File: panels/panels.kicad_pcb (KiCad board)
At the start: 2 copper layers, 103 x 63 mm, 13 parts, among them J1 Barrel_Jack_Switch, J2 Barrel_Jack_Switch, J3 Barrel_Jack_Switch, J4 Barrel_Jack_Switch, J5 XLR3

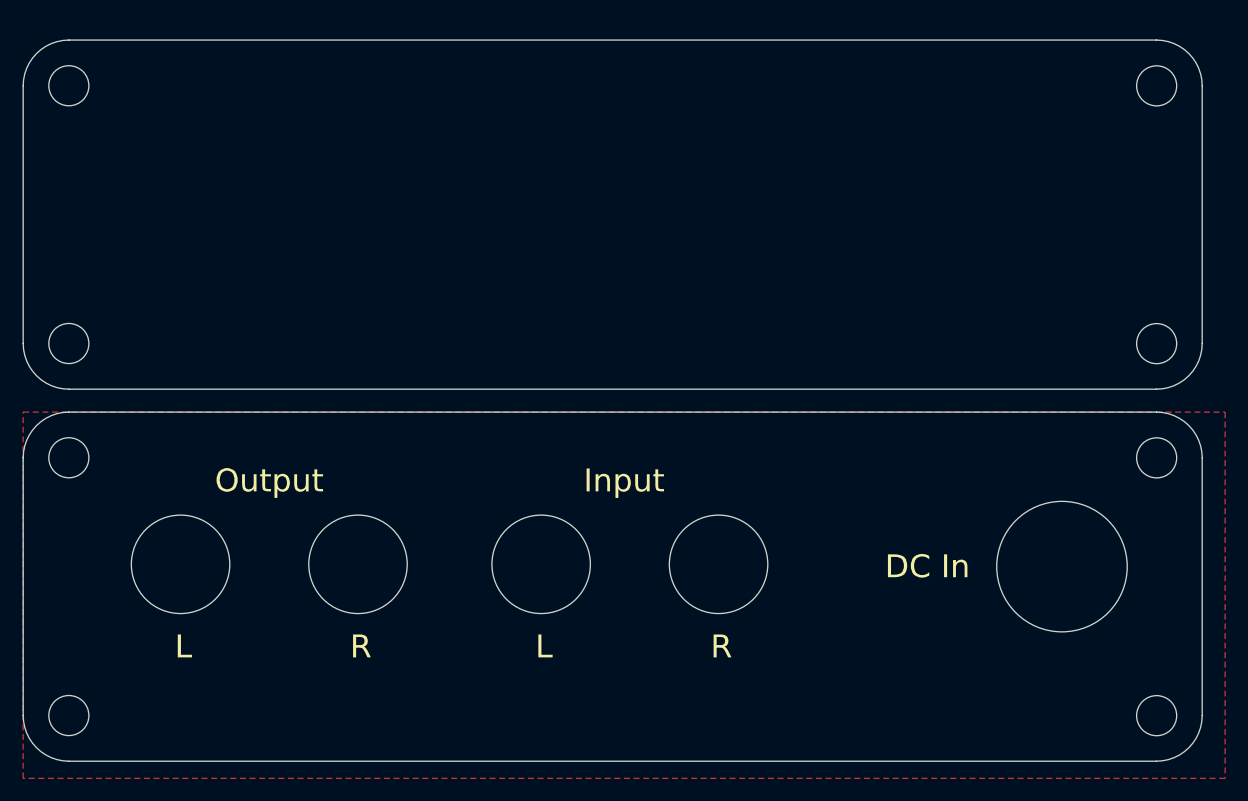
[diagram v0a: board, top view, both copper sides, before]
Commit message: Update panels with custom footprints
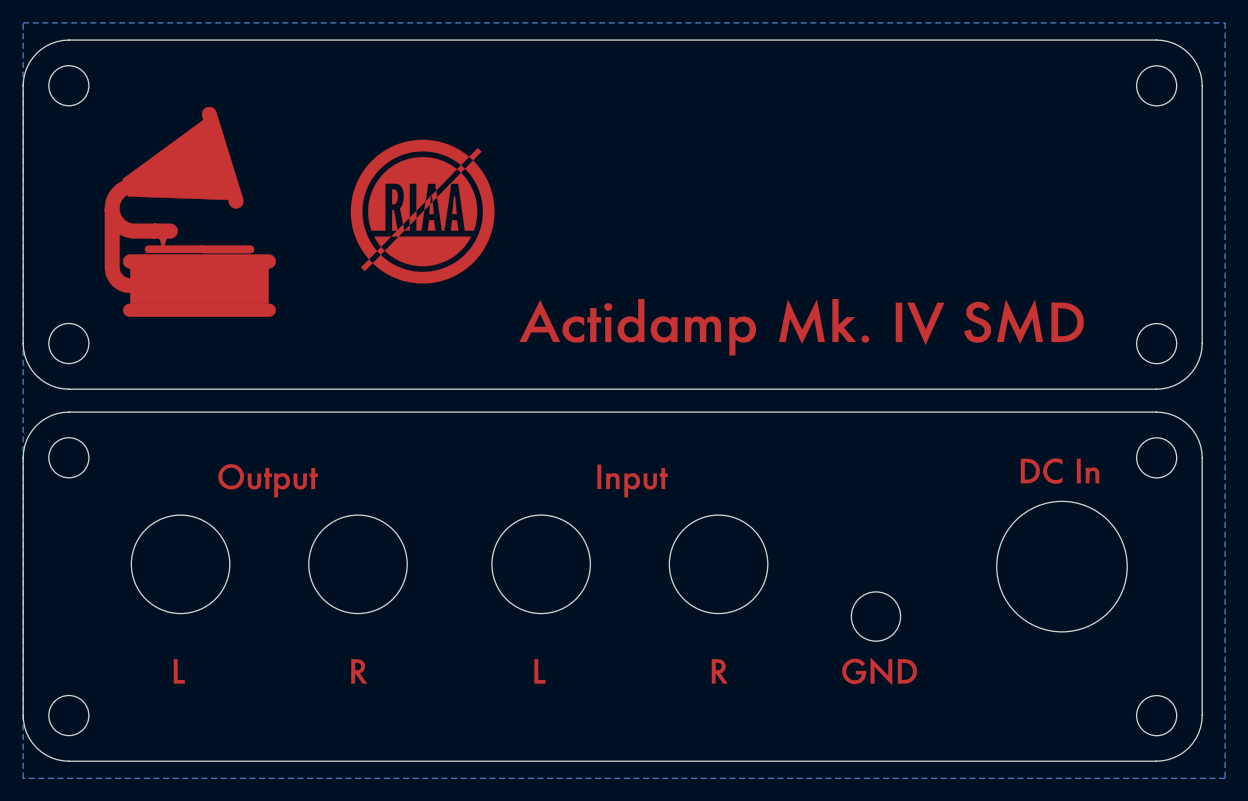
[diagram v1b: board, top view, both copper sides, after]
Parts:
- added Grp1: Logos, actidamp-mk4-smd:FP_Logo, F.Cu at (70.0, 74.0)
- added Grp10: DC In, actidamp-mk4-smd:BP_text_DC_In, F.Cu at (146.5, 95.5)
- added Grp2: Text, actidamp-mk4-smd:FP_text, F.Cu at (123.0, 82.0)
- added Grp3: L, actidamp-mk4-smd:BP_text_L, F.Cu at (72.5, 113.0)
- added Grp4: Output, actidamp-mk4-smd:BP_text_output, F.Cu at (76.5, 96.0)
- added Grp5: R, actidamp-mk4-smd:BP_text_R, F.Cu at (88.0, 113.0)
- added Grp6: L, actidamp-mk4-smd:BP_text_L, F.Cu at (104.0, 113.0)
- added Grp7: Input, actidamp-mk4-smd:BP_text_input, F.Cu at (109.5, 96.0)
- added Grp8: R, actidamp-mk4-smd:BP_text_R, F.Cu at (119.5, 113.0)
- added Grp9: GND, actidamp-mk4-smd:BP_text_GND, F.Cu at (131.0, 113.0)
- added H9: GroundLug, MountingHole:MountingHole_4.3mm_M4, F.Cu at (129.5, 107.9)
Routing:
- added copper zone on B.Cu, net (none)
- removed copper zone on F.Cu, net (none)
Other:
- board text removed: "DC In"
- board text removed: "Input"
- board text removed: "L"
- board text removed: "Output"
- board text removed: "R"

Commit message: Use only mask layer for FB/BP
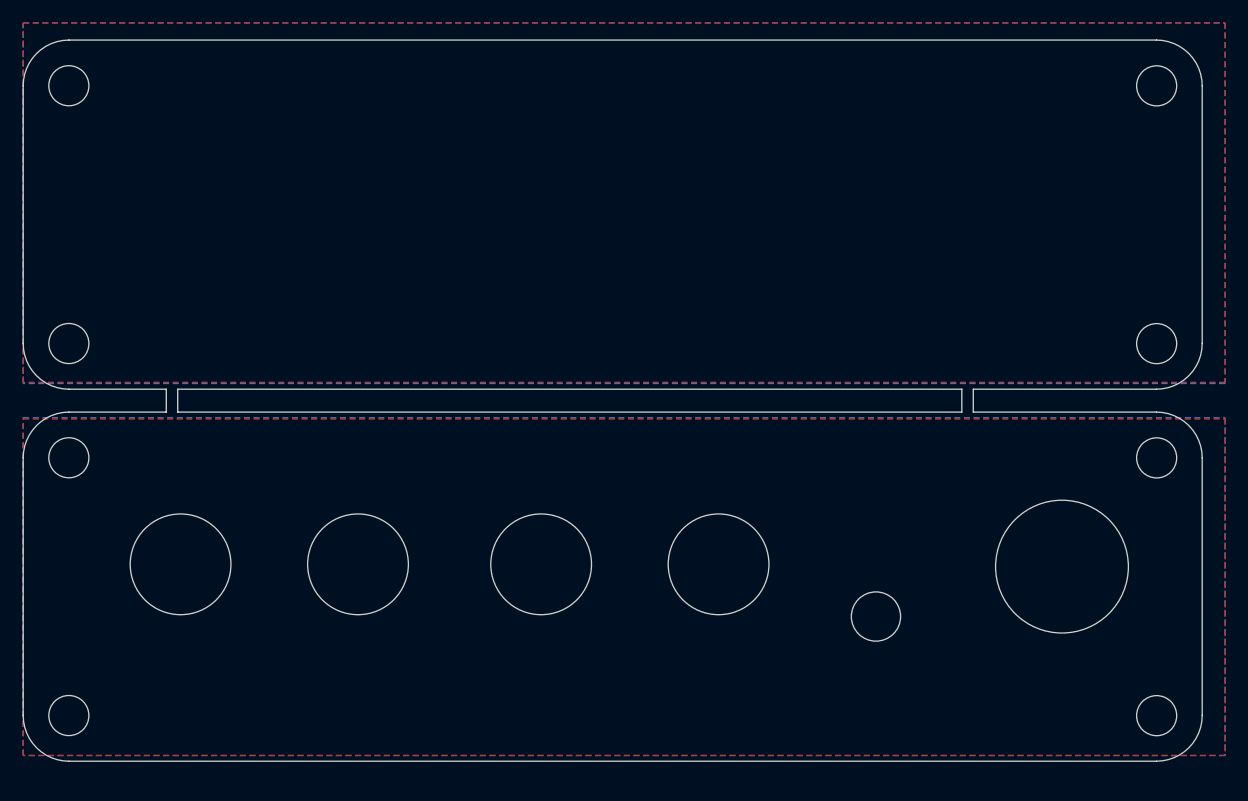
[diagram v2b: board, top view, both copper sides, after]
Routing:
- added copper zone on F.Cu, net (none)
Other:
- outline, holes or cut-outs redrawn
- rule pad_to_mask_clearance: 0.051 -> 0.02

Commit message: Add custom JLC number to bottom silkscreen
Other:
- board text added: "JLCJLCJLCJLC"
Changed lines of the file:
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@@
   (general
     (thickness 1.6)
-    (drawings 24)
+    (drawings 25)
     (tracks 0)
     (zones 0)
@@
       (xy -1.573644 -1.419745) (xy -1.42059 -1.445353) (xy -1.27635 -1.452417) (xy -1.177522 -1.450504)) (layer F.Mask) (width 0.01))
   )
+  (gr_text JLCJLCJLCJLC (at 112.8 71.7) (layer B.SilkS)
+    (effects (font (size 1.2 1.2) (thickness 0.15)) (justify mirror))
+  )
   (gr_line (start 67.5 88) (end 59 88) (layer Edge.Cuts) (width 0.05))
